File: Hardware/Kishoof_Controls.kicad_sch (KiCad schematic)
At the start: 30 parts, among them J1 Conn_01x12_Pin, J10 Audio_Out_L, J11 Audio_Out_R, J12 USB_C_Receptacle, J14 Conn_01x01_Socket, J2 Conn_01x12_Pin, J3 Conn_01x10_Pin, J4 Conn_01x10_Pin, J5 WavetablePosA, J6 WavetablePosB, J7 WarpCV, J8 VOct, J9 VCA, SW1 SW_Push, SW2 Mode_Switch, SW3 Octave_Switch, SW4 ChB_Output, SW5 Encoder, U1 STF202-22T1G

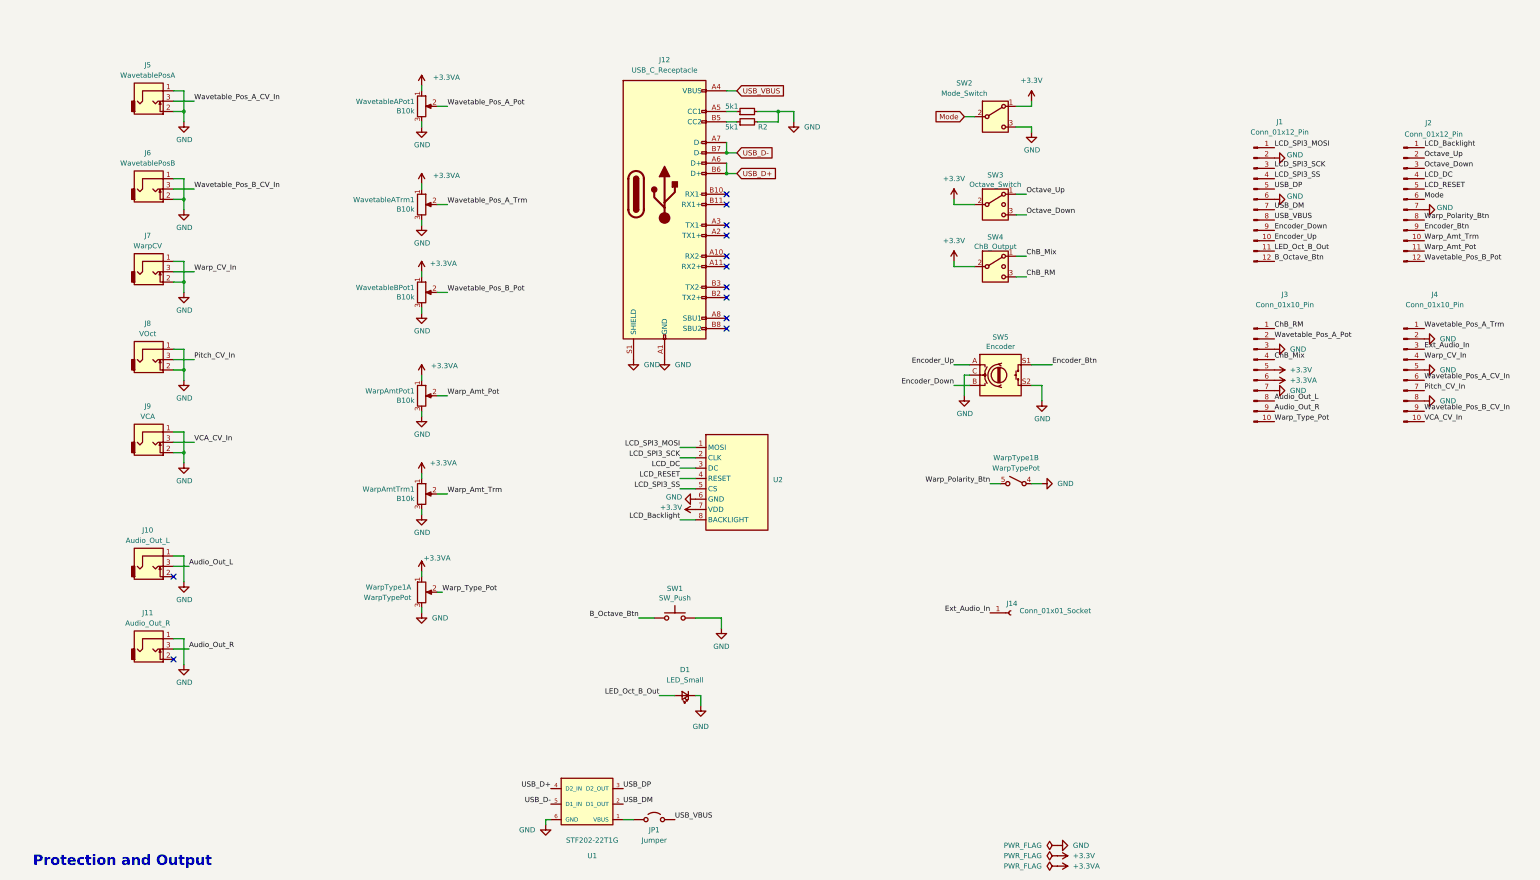
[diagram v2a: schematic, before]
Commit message: PCBs v1.0 ordered
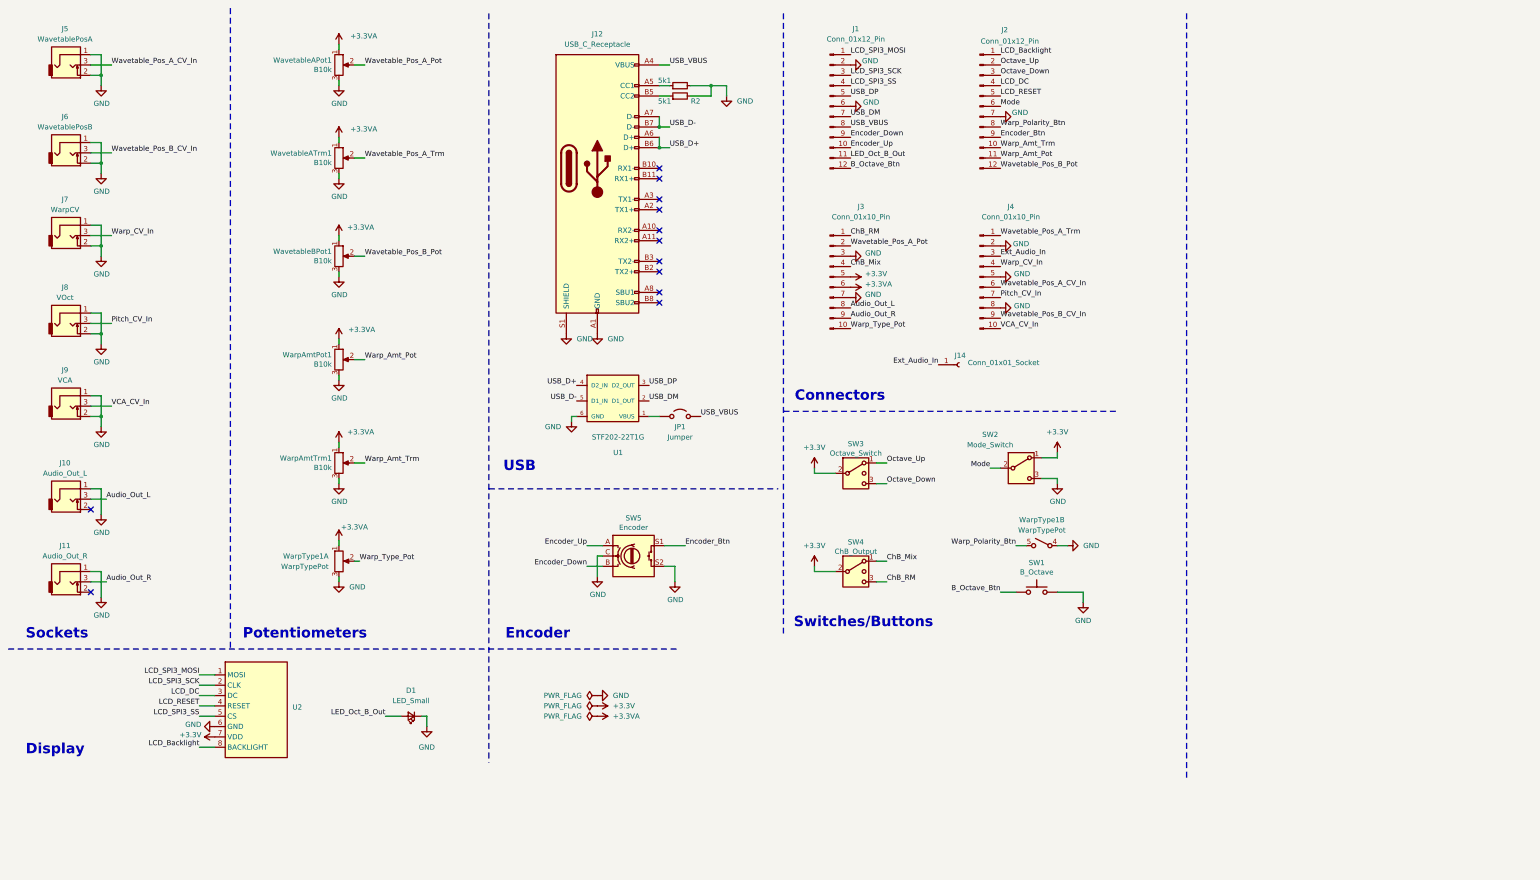
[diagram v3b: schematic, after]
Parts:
- SW1: value SW_Push -> B_Octave
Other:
- note added: "Connectors"
- note added: "Display"
- note added: "Encoder"
- note added: "Potentiometers"
- note added: "Sockets"
- note added: "Switches/Buttons"
- note added: "USB"
- note removed: "Protection and Output"
- moved on the sheet: D1, J1, J10, J11, J12, J14, J2, J3, J4, J5, J6, J7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

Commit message: Tweaks to get USB CDC working
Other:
- note added: "Errata: Warp Switched POt has incorrect mounting hole sizes (now fixed in library)"
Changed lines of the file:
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@@
+		)
+	)
+	(text "Errata: Warp Switched POt has incorrect mounting hole sizes (now fixed in library)"
+		(exclude_from_sim no)
+		(at 222.25 170.434 0)
+		(effects
+			(font
+				(size 1.27 1.27)
+			)
 		)
 	)

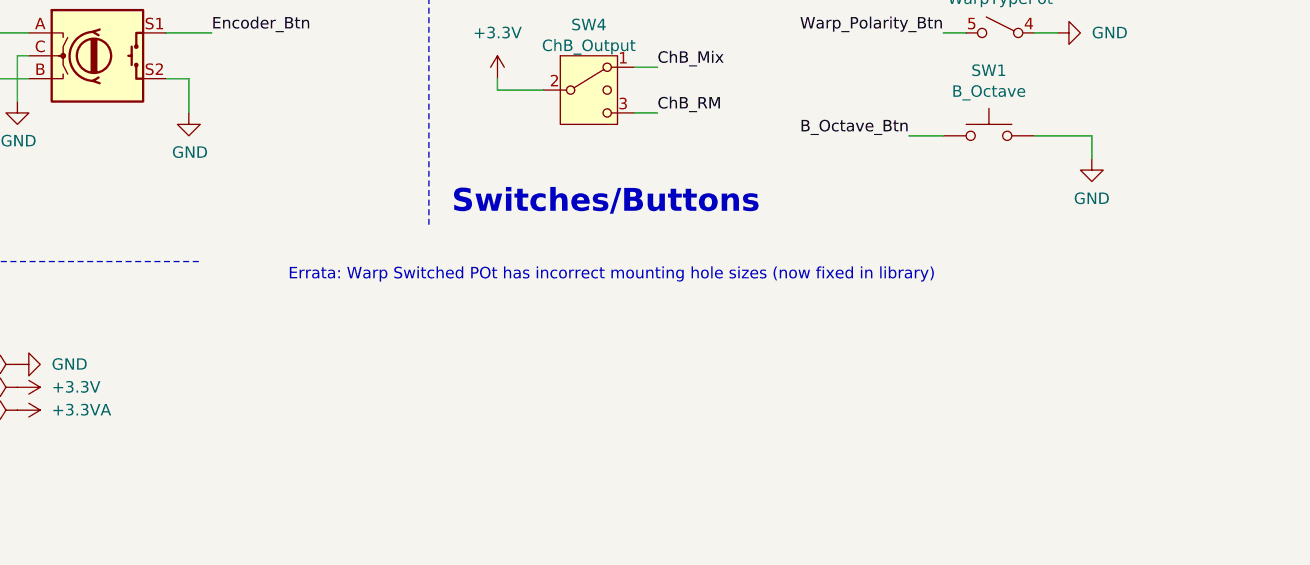
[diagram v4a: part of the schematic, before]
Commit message: USB flash reads don't use MDMA to resolve USB reads hanging
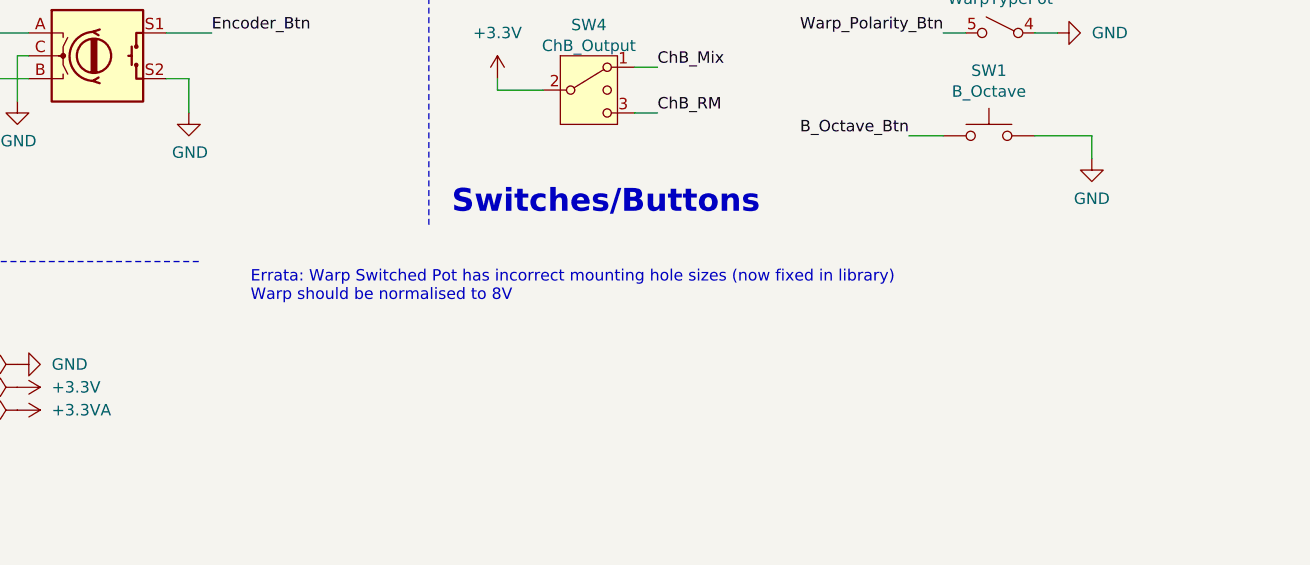
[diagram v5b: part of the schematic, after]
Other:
- note added: "Errata: Warp Switched Pot has incorrect mounting hole sizes (now fixed in library) Warp should be normalised to 8V"
- note removed: "Errata: Warp Switched POt has incorrect mounting hole sizes (now fixed in library)"
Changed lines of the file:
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@@
 		)
 	)
-	(text "Errata: Warp Switched POt has incorrect mounting hole sizes (now fixed in library)"
+	(text "Errata: Warp Switched Pot has incorrect mounting hole sizes (now fixed in library)\nWarp should be normalised to 8V"
 		(exclude_from_sim no)
-		(at 222.25 170.434 0)
+		(at 182.118 171.704 0)
 		(effects
 			(font
 				(size 1.27 1.27)
 			)
+			(justify left)
 		)
 	)

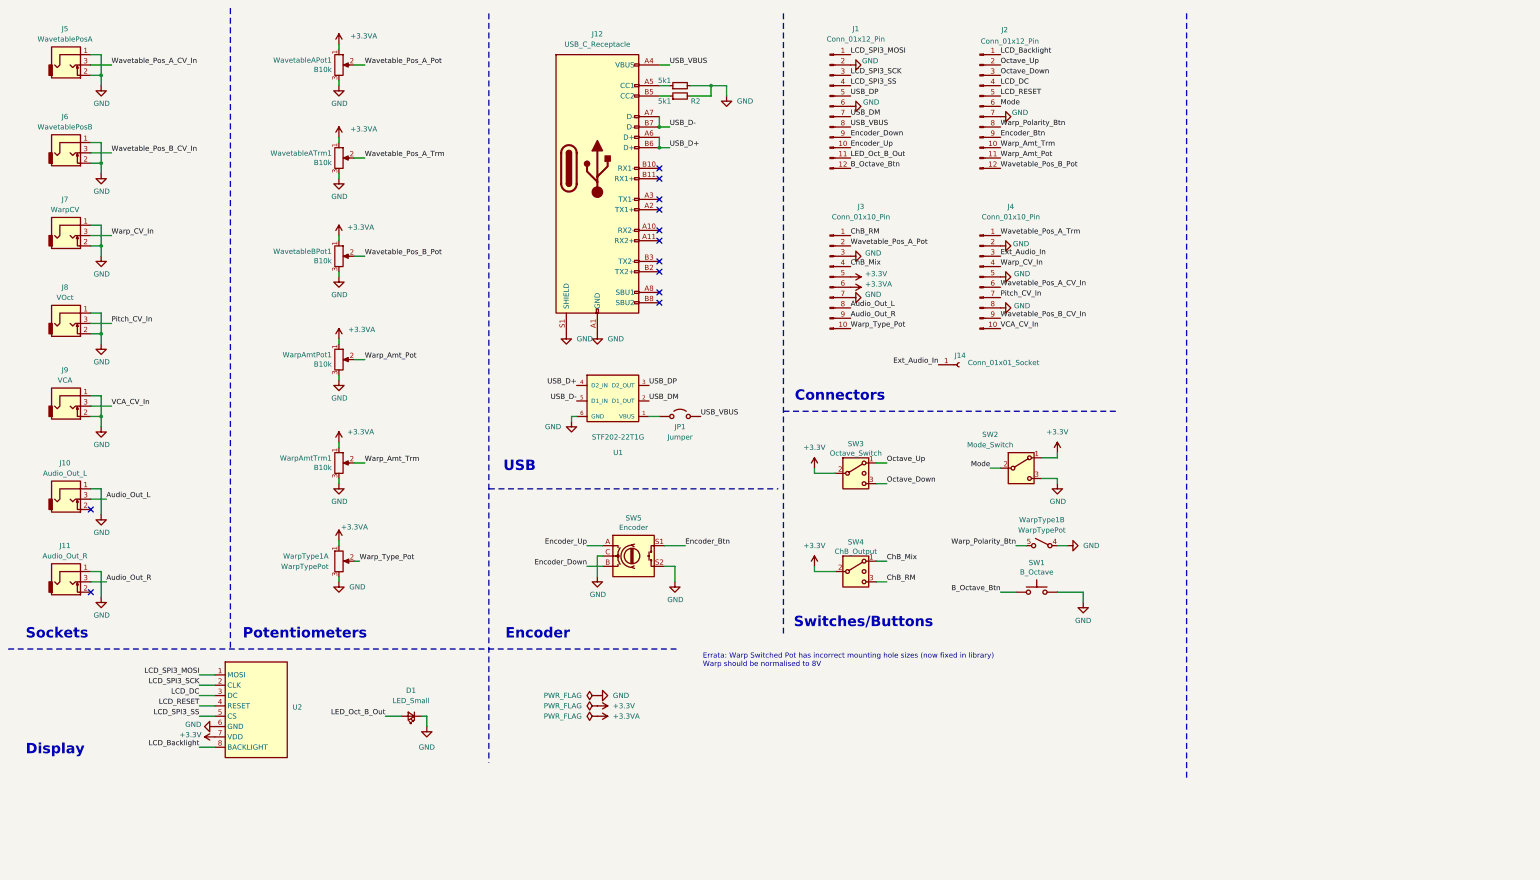
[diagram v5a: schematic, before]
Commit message: Updated Controls PCB to fix VCA normalisation problem
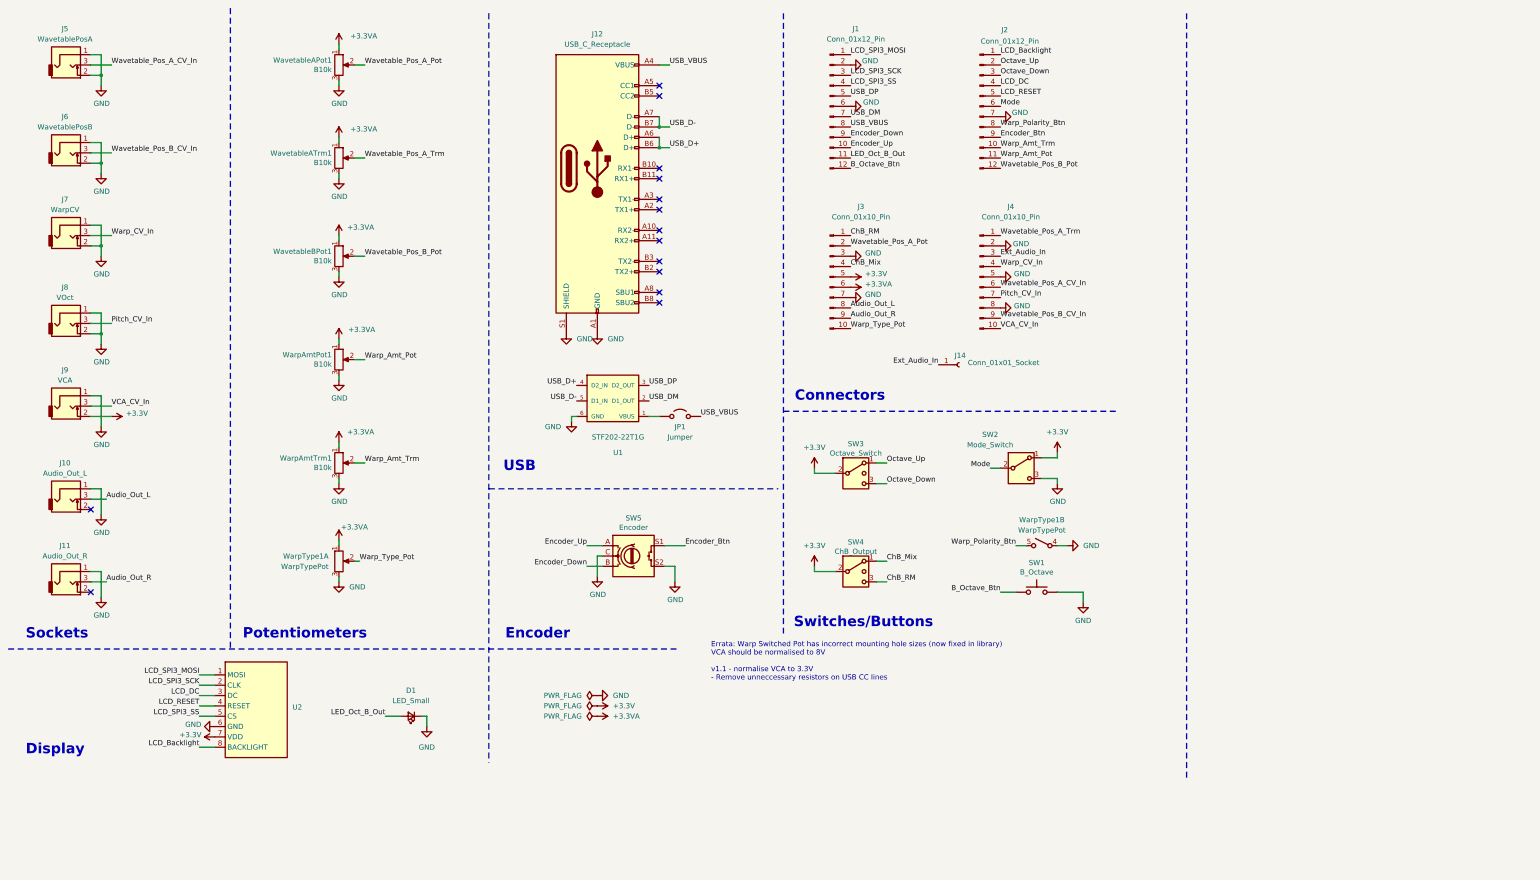
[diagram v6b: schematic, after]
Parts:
- removed R1, R2: 5k1, Resistor_SMD:R_0603_1608Metric, symbol Device:R_Small
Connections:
- net +3.3V: now also J9.2
- net GND: no longer J9.2
- no-connect marks 12 -> 14
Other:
- note added: "Errata: Warp Switched Pot has incorrect mounting hole sizes (now fixed in library) VCA should be normalised to 8V v1.1 - normalise VCA to 3.3V - Remove unneccessary resistors on USB CC lines"
- note removed: "Errata: Warp Switched Pot has incorrect mounting hole sizes (now fixed in library) Warp should be normalised to 8V"
